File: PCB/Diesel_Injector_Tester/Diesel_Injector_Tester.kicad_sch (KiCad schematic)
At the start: 35 parts, among them J1 PWR, J2 INJECTOR, J3 PROG, Q1 IRLR8726, SW1 ENABLE, SW2 PERIOD, U1 LM1117DT-3.3, U2 STM32F030F4Px, U3 MCP1416, Y1 8MHz

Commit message: PCB prepared, schematic updated
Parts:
- C10, C11, C12, C3, C4, C6, C7, C8, C9: footprint Capacitor_SMD:C_1206_3216Metric_Pad1.33x1.80mm_HandSolder -> Capacitor_SMD:C_0805_2012Metric_Pad1.18x1.45mm_HandSolder
- D3: value GREEN -> PWR_GREEN
- D4: value GREEN -> ENABLE_GREEN
- D5: value GREEN -> PERIOD_GREEN
- J3: footprint Connector_PinSocket_2.54mm:PinSocket_1x04_P2.54mm_Horizontal -> Connector_PinSocket_2.54mm:PinSocket_1x04_P2.54mm_Vertical
- R1, R2, R3, R4, R5, R6, R7, R8: footprint Resistor_SMD:R_1206_3216Metric_Pad1.30x1.75mm_HandSolder -> Resistor_SMD:R_0805_2012Metric_Pad1.20x1.40mm_HandSolder
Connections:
- net ENABLE_KEY: now also U2.9 (PA3); no longer U2.8 (PA2)
- net PERIOD_KEY: now also U2.8 (PA2); no longer U2.9 (PA3)
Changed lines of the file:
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@@
 (kicad_sch
-	(version 20231120)
+	(version 20250114)
 	(generator "eeschema")
-	(generator_version "8.0")
+	(generator_version "9.0")
 	(paper "A4")
 	(title_block
@@
 		(company "trwgQ26xxx")
 	)
+	(text "PIN1 is: GND for MCP1402(0.5A), NC for MCP1416(1.5A)"
+		(exclude_from_sim no)
+		(at 225.552 128.016 0)
+		(effects
+			(font
+				(size 1.27 1.27)
+			)
+		)
+	)
 	(junction
 		(at 201.93 109.22)
@@
 		)
 	)
-	(text "PIN1 is: GND for MCP1402(0.5A), NC for MCP1416(1.5A)"
-		(exclude_from_sim no)
-		(at 225.552 128.016 0)
-		(effects
-			(font
-				(size 1.27 1.27)
-			)
-		)
-	)
 	(global_label "SWDIO"
 		(shape input)
@@
 		)
 	)
-	(global_label "PERIOD_KEY"
-		(shape input)
-		(at 135.89 90.17 0)
-		(fields_autoplaced yes)
-		(effects
-			(font
-				(size 1.27 1.27)
-			)
-			(justify left)
-		)
-		(property "Intersheetrefs" "${INTERSHEET_REFS}"
-			(at 150.2447 90.17 0)
-			(effects
-				(font
-					(size 1.27 1.27)
-				)
-				(justify left)
-				(hide yes)
-			)
-		)
-	)
 	(global_label "ENABLE_KEY"
 		(shape input)
-		(at 135.89 87.63 0)
+		(at 135.89 90.17 0)
 		(fields_autoplaced yes)
 		(effects
@@
 		)
 		(property "Intersheetrefs" "${INTERSHEET_REFS}"
-			(at 150.3656 87.63 0)
+			(at 150.3656 90.17 0)
 			(effects
 				(font
@@
 		)
 	)
+	(global_label "PERIOD_KEY"
+		(shape input)
+		(at 135.89 87.63 0)
+		(fields_autoplaced yes)
+		(effects
+			(font
+				(size 1.27 1.27)
+			)
+			(justify left)
+		)
+		(property "Intersheetrefs" "${INTERSHEET_REFS}"
+			(at 150.2447 87.63 0)
+			(effects
+				(font
+					(size 1.27 1.27)
+				)
+				(justify left)
+				(hide yes)
+			)
+		)
+	)
 	(global_label "INJ_PULSES"
 		(shape input)
@@
 			)
 		)
-		(property "Footprint" "Resistor_SMD:R_1206_3216Metric_Pad1.30x1.75mm_HandSolder"
+		(property "Footprint" "Resistor_SMD:R_0805_2012Metric_Pad1.20x1.40mm_HandSolder"
 			(at 130.302 161.29 90)
 			(effects
@@
 			)
 		)
-		(property "Footprint" "Capacitor_SMD:C_1206_3216Metric_Pad1.33x1.80mm_HandSolder"
+		(property "Footprint" "Capacitor_SMD:C_0805_2012Metric_Pad1.18x1.45mm_HandSolder"
 			(at 42.8752 172.72 0)
 			(effects
@@
 			)
 		)
-		(property "Footprint" "Resistor_SMD:R_1206_3216Metric_Pad1.30x1.75mm_HandSolder"
+		(property "Footprint" "Resistor_SMD:R_0805_2012Metric_Pad1.20x1.40mm_HandSolder"
 			(at 200.152 114.3 90)
 			(effects
@@
 			)
 		)
-		(property "Footprint" "Capacitor_SMD:C_1206_3216Metric_Pad1.33x1.80mm_HandSolder"
+		(property "Footprint" "Capacitor_SMD:C_0805_2012Metric_Pad1.18x1.45mm_HandSolder"
 			(at 70.8152 111.76 0)
 			(effects
@@
 			)
 		)
-		(property "Value" "GREEN"
+		(property "Value" "PERIOD_GREEN"
 			(at 160.02 174.3074 90)
 			(effects
@@
 			)
 		)
-		(property "Footprint" "Resistor_SMD:R_1206_3216Metric_Pad1.30x1.75mm_HandSolder"
+		(property "Footprint" "Resistor_SMD:R_0805_2012Metric_Pad1.20x1.40mm_HandSolder"
 			(at 28.702 154.94 90)
 			(effects
@@
 			)
 		)
-		(property "Footprint" "Resistor_SMD:R_1206_3216Metric_Pad1.30x1.75mm_HandSolder"
+		(property "Footprint" "Resistor_SMD:R_0805_2012Metric_Pad1.20x1.40mm_HandSolder"
 			(at 62.992 154.94 90)
 			(effects
@@
 			)
 		)
-		(property "Footprint" "Capacitor_SMD:C_1206_3216Metric_Pad1.33x1.80mm_HandSolder"
+		(property "Footprint" "Capacitor_SMD:C_0805_2012Metric_Pad1.18x1.45mm_HandSolder"
 			(at 77.1652 172.72 0)
 			(effects
@@
 			)
 		)
-		(property "Footprint" "Resistor_SMD:R_1206_3216Metric_Pad1.30x1.75mm_HandSolder"
+		(property "Footprint" "Resistor_SMD:R_0805_2012Metric_Pad1.20x1.40mm_HandSolder"
 			(at 236.22 110.998 90)
 			(effects
@@
 			)
 		)
-		(property "Value" "GREEN"
+		(property "Value" "ENABLE_GREEN"
 			(at 135.89 174.3074 90)
 			(effects
@@
 			)
 		)
-		(property "Footprint" "Resistor_SMD:R_1206_3216Metric_Pad1.30x1.75mm_HandSolder"
+		(property "Footprint" "Resistor_SMD:R_0805_2012Metric_Pad1.20x1.40mm_HandSolder"
 			(at 106.172 161.29 90)
 			(effects
@@
 			)
 		)
-		(property "Value" "GREEN"
+		(property "Value" "PWR_GREEN"
 			(at 111.76 174.3074 90)
 			(effects
@@
 			)
 		)
-		(property "Footprint" "Capacitor_SMD:C_1206_3216Metric_Pad1.33x1.80mm_HandSolder"
+		(property "Footprint" "Capacitor_SMD:C_0805_2012Metric_Pad1.18x1.45mm_HandSolder"
 			(at 97.4852 41.91 0)
 			(effects
@@
 			)
 		)
-		(property "Footprint" "Capacitor_SMD:C_1206_3216Metric_Pad1.33x1.80mm_HandSolder"
+		(property "Footprint" "Capacitor_SMD:C_0805_2012Metric_Pad1.18x1.45mm_HandSolder"
 			(at 224.4852 92.71 0)
 			(effects
@@
 			)
 		)
-		(property "Footprint" "Capacitor_SMD:C_1206_3216Metric_Pad1.33x1.80mm_HandSolder"
+		(property "Footprint" "Capacitor_SMD:C_0805_2012Metric_Pad1.18x1.45mm_HandSolder"
 			(at 96.2152 111.76 0)
 			(effects
@@
 			)
 		)
-		(property "Footprint" "Capacitor_SMD:C_1206_3216Metric_Pad1.33x1.80mm_HandSolder"
+		(property "Footprint" "Capacitor_SMD:C_0805_2012Metric_Pad1.18x1.45mm_HandSolder"
 			(at 138.1252 73.66 0)
 			(effects
@@
 			)
 		)
-		(property "Footprint" "Connector_PinSocket_2.54mm:PinSocket_1x04_P2.54mm_Horizontal"
+		(property "Footprint" "Connector_PinSocket_2.54mm:PinSocket_1x04_P2.54mm_Vertical"
 			(at 40.64 110.49 0)
 			(effects
@@
 			)
 		)
-		(property "Footprint" "Capacitor_SMD:C_1206_3216Metric_Pad1.33x1.80mm_HandSolder"
+		(property "Footprint" "Capacitor_SMD:C_0805_2012Metric_Pad1.18x1.45mm_HandSolder"
 			(at 83.5152 111.76 0)
 			(effects
@@
 			)
 		)
-		(property "Footprint" "Capacitor_SMD:C_1206_3216Metric_Pad1.33x1.80mm_HandSolder"
+		(property "Footprint" "Capacitor_SMD:C_0805_2012Metric_Pad1.18x1.45mm_HandSolder"
 			(at 124.1552 41.91 0)
 			(effects
@@
 			)
 		)
-		(property "Footprint" "Resistor_SMD:R_1206_3216Metric_Pad1.30x1.75mm_HandSolder"
+		(property "Footprint" "Resistor_SMD:R_0805_2012Metric_Pad1.20x1.40mm_HandSolder"
 			(at 154.432 161.29 90)
 			(effects
@@
 			)
 		)
-		(property "Footprint" "Resistor_SMD:R_1206_3216Metric_Pad1.30x1.75mm_HandSolder"
+		(property "Footprint" "Resistor_SMD:R_0805_2012Metric_Pad1.20x1.40mm_HandSolder"
 			(at 68.072 71.12 90)
 			(effects
@@
 		)
 	)
+	(embedded_fonts no)
 )

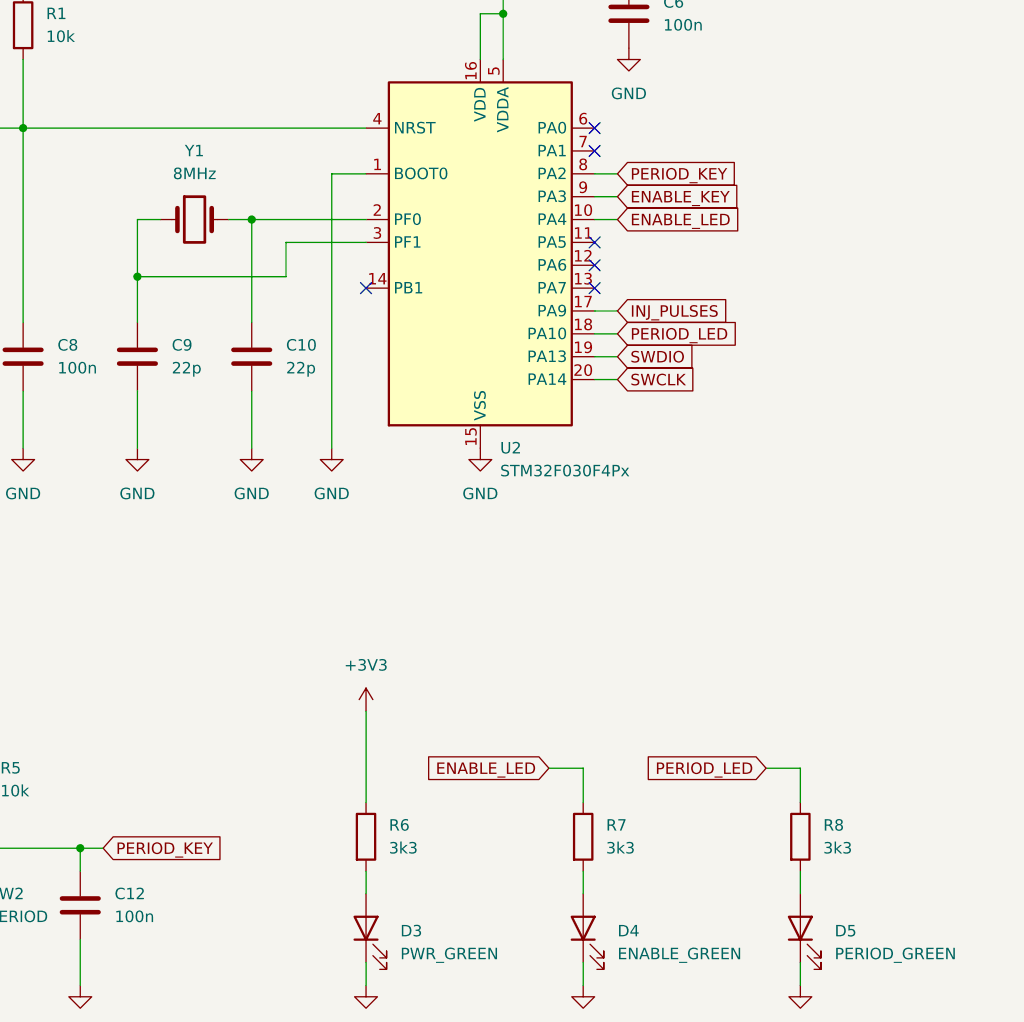
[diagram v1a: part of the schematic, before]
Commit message: Schematic updated for final component values
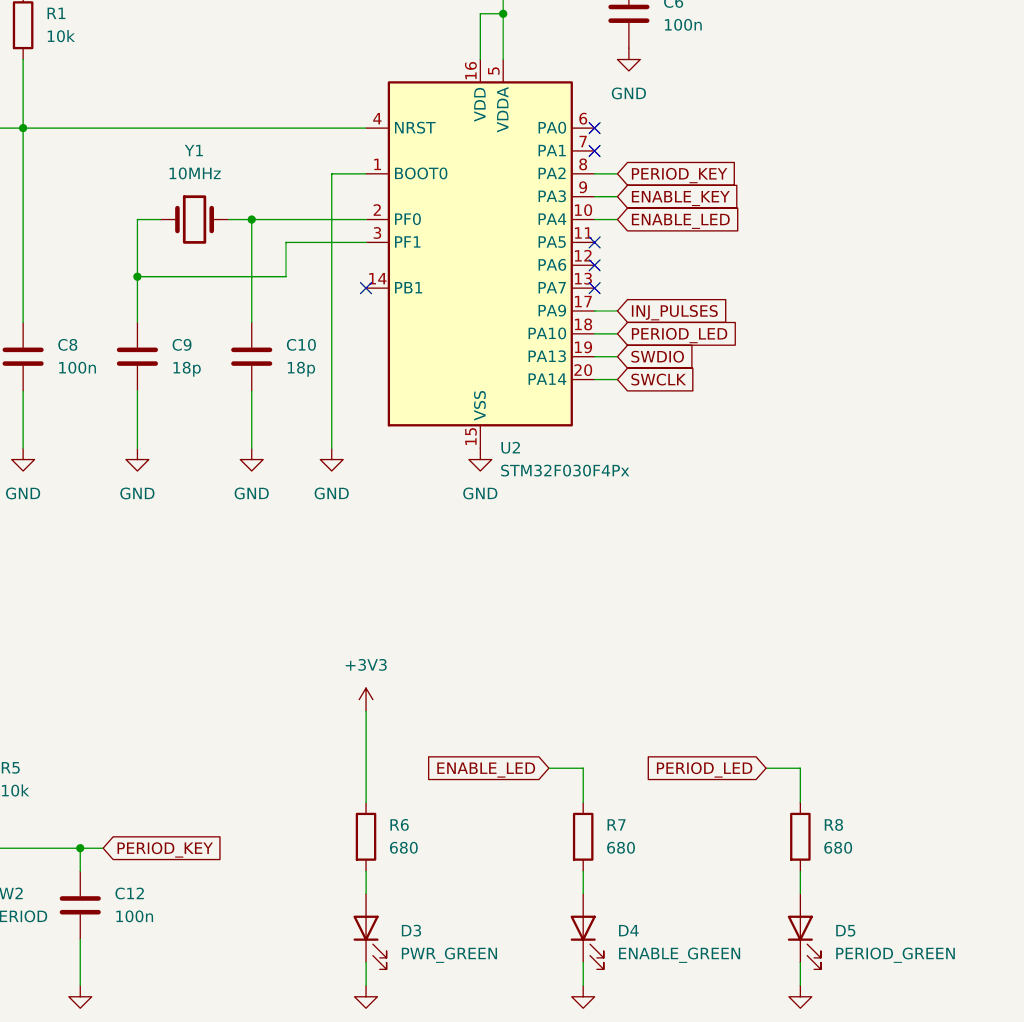
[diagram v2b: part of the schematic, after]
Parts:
- C10, C9: value 22p -> 18p
- R6, R7, R8: value 3k3 -> 680
- Y1: value 8MHz -> 10MHz
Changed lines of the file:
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@@
 			)
 		)
-		(property "Value" "3k3"
+		(property "Value" "680"
 			(at 134.62 162.5599 0)
 			(effects
@@
 			)
 		)
-		(property "Value" "3k3"
+		(property "Value" "680"
 			(at 110.49 162.5599 0)
 			(effects
@@
 			)
 		)
-		(property "Value" "8MHz"
+		(property "Value" "10MHz"
 			(at 88.9 87.63 0)
 			(effects
@@
 		(fields_autoplaced yes)
 		(property "Reference" "C10"
-			(at 99.06 106.68 0)
+			(at 99.06 106.6799 0)
 			(effects
 				(font
@@
 			)
 		)
-		(property "Value" "22p"
-			(at 99.06 109.22 0)
+		(property "Value" "18p"
+			(at 99.06 109.2199 0)
 			(effects
 				(font
@@
 		(fields_autoplaced yes)
 		(property "Reference" "C9"
-			(at 86.36 106.68 0)
+			(at 86.36 106.6799 0)
 			(effects
 				(font
@@
 			)
 		)
-		(property "Value" "22p"
-			(at 86.36 109.22 0)
+		(property "Value" "18p"
+			(at 86.36 109.2199 0)
 			(effects
 				(font
@@
 			)
 		)
-		(property "Value" "3k3"
+		(property "Value" "680"
 			(at 158.75 162.5599 0)
 			(effects
